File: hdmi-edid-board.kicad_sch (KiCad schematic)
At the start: 0 parts

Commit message: [#77357] Clean up schematics
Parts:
- added C1, C2: C_10u_0603, antmicro-footprints:C_0603_1608Metric, symbol antmicroCapacitors0603:C_10u_0603
- added C10, C14, C15, C16, C19, C20, C21, C22, C24, C4, C5, C6, C7, C8: C_100n_16V_X7R_0402, antmicro-footprints:C_0402_1005Metric, symbol antmicroCapacitors0402:C_100n_16V_X7R_0402
- added C11, C17, C18, C23: C_4u7_0402, antmicro-footprints:C_0402_1005Metric, symbol antmicroCapacitors0402:C_4u7_0402
- added C12, C13, C9: C_1u_0603, antmicro-footprints:C_0603_1608Metric, symbol antmicroCapacitors0603:C_1u_0603
- added C3: C_10n_0402, antmicro-footprints:C_0402_1005Metric, symbol antmicroCapacitors0402:C_10n_0402
- added D1, D3: PESD5Z5_0F, antmicro-footprints:SOD-523, symbol antmicroTVSDiodes:PESD5Z5_0F
- added D2: LED_G_0603_LTST-C190GKT, antmicro-footprints:LED_0603_1608Metric_G, symbol antmicroLEDIndicationDiscrete:LED_G_0603_LTST-C190GKT
- added D4: TPD2E009_SOT-9X3, antmicro-footprints:SOT-723, symbol antmicroTVSDiodes:TPD2E009_SOT-9X3
- added D5: BAT54-02V-G3-08, antmicro-footprints:SOD-523, symbol antmicroDiodesRectifiersSingle:BAT54-02V-G3-08
- added FB1, FB2: FB_220Z_2.2A_TDK-MPZ_0603, antmicro-footprints:FB_0603_1608Metric, symbol antmicroFerriteBeadsandChips:FB_220Z_2.2A_TDK-MPZ_0603
- added FB3, FB4: FB_600Z_0.3A_Murata-BLM15AG_0402, antmicro-footprints:FB_0402_1005Metric, symbol antmicroFerriteBeadsandChips:FB_600Z_0.3A_Murata-BLM15AG_0402
- added J1, J4: HDMI-A_WE_685119134923, antmicro-footprints:HDMI-A_Receptacle_WE_685119134923, symbol antmicroVideoConnectors:HDMI-A_WE_685119134923
- added J2, J3: PinHeader_2x2_P2.54mm_Drill1.1mm, antmicro-footprints:PinHeader_2x2_P2.54mm_Drill1.1mm, symbol antmicroGenericPinHeaders:PinHeader_2x2_P2.54mm_Drill1.1mm
- added J5: USB-C_GCT_USB4105-GF-A, antmicro-footprints:USB-C_Receptacle_GCT_USB4105-GF-A, symbol antmicroUSBConnectors:USB-C_GCT_USB4105-GF-A
- added J6: JST_SH_1x4_SM04B-SRSS-TB-LF-SN, antmicro-footprints:Conn_JST_SH_1x4_SM04B-SRSS-TB-LF-SN, symbol antmicroWire2BoardConnectors:JST_SH_1x4_SM04B-SRSS-TB-LF-SN
- added L1, L2: FB_120Z_2A_Murata-BLM18PG_0603, antmicro-footprints:FB_0603_1608Metric, symbol antmicroFerriteBeadsandChips:FB_120Z_2A_Murata-BLM18PG_0603
- added R1: R_330R_0603, antmicro-footprints:R_0603_1608Metric, symbol antmicroResistors0603:R_330R_0603
- added R10, R11: R_5k1_0402, antmicro-footprints:R_0402_1005Metric, symbol antmicroResistors0402:R_5k1_0402
- added R12: R_470R_0402, antmicro-footprints:R_0402_1005Metric, symbol antmicroResistors0402:R_470R_0402
- added R13, R14, R15: R_220R_0402, antmicro-footprints:R_0402_1005Metric, symbol antmicroResistors0402:R_220R_0402
- added R16: R_4k7_0402, antmicro-footprints:R_0402_1005Metric, symbol antmicroResistors0402:R_4k7_0402
- added R17: R_10k_0402, antmicro-footprints:R_0402_1005Metric, symbol antmicroResistors0402:R_10k_0402
- added R18: R_12k_0402, antmicro-footprints:R_0402_1005Metric, symbol antmicroResistors0402:R_12k_0402
- added R19, R2, R20, R21, R3, R4, R5, R6, R7, R8, R9: R_0R_0402, antmicro-footprints:R_0402_1005Metric, symbol antmicroResistors0402:R_0R_0402
- added TP1, TP2: TP_1.5mm_SMD, antmicro-footprints:TP_SMD_1.5mm, symbol antmicroTestPoints:TP_1.5mm_SMD
- added U1: 24LC02BT-I/SN, antmicro-footprints:SOIC-8_3.9x4.9x1.75mm_P1.27mm, symbol antmicroMemory:24LC02BT-I/SN
- added U2: 24AA024T-I/SN, antmicro-footprints:SOIC-8_3.9x4.9x1.75mm_P1.27mm, symbol antmicroMemory:24AA024T-I/SN
- added U3: NTS0302JKZ, antmicro-footprints:X2SON8_1.4x1x0.32mm_P0.35mm, symbol antmicroLogicTranslatorsLevelShifters:NTS0302JKZ
- added U4: TLV70033_SC70, antmicro-footprints:SC-70-5, symbol antmicroPMICVoltageRegulatorsLinear:TLV70033_SC70
- added U5: FT4232H_VQFN, antmicro-footprints:QFN-56-1EP_8x8mm_P0.5mm, symbol antmicroInterfaceControllers:FT4232H_VQFN
- added USB1: LED_G_0603_LG_L29K-G2J1-24-Z, antmicro-footprints:LED_0603_1608Metric_G, symbol antmicroLEDIndicationDiscrete:LED_G_0603_LG_L29K-G2J1-24-Z
- added Y1: Oscillator_12MHz_ASFLMB, antmicro-footprints:Oscillator_SMD_Abracon_ASFLMB_5x3.2x0.85mm, symbol antmicroOscillators:Oscillator_12MHz_ASFLMB
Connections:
- new net: C11.2, D5.2 (A), R15.1, U3.1 (VCC_A)
- new net: C3.1, J5.A4 (VBUS), J5.A9 (VBUS), J5.B4 (VBUS), J5.B9 (VBUS), L2.2
- new net: J5.A5 (CC_{1}), R10.1
- new net: J5.B5 (CC_{2}), R11.1
- new net: C1.2, D1.1 (C), FB1.1, J1.18 (+5V)
- new net: R12.2, USB1.1 (C)
- new net: R13.1, U3.2 (A1)
- new net: R14.1, U3.3 (A2)
- new net: R19.1, U5.22 (BDBUS0)
- new net: C2.2, D3.1 (C), FB2.2, J4.18 (+5V)
- new net: R18.1, U5.6 (REF)
- new net: R21.1, U5.24 (BDBUS2)
- new net: D2.1 (C), R1.2
- new net: R20.1, U5.23 (BDBUS1)
- new net +3V3: C10.1, C12.1, C13.1, C14.1, C15.1, C16.1, C20.1, C24.1, D5.1 (C), FB3.1, FB4.1, J6.2, U3.5 (OE), U3.8 (VCC_B), U4.5 (VOUT), U5.16 (V_{CCIO}), U5.36 (V_{CCIO}), U5.44 (V_{REGIN}), U5.50 (V_{CCIO}), Y1.1 (EN), Y1.4 (VDD)
- new net +5V: C6.1, C7.1, C8.1, C9.1, L2.1, R15.2, R16.2, R4.2, R6.2, R8.2, U4.1 (VIN), U4.3 (EN), USB1.2 (A)
- new net A0: R4.1, R5.2, U2.1 (A0)
- new net A1: R6.1, R7.2, U2.2 (A1)
- new net A2: R8.1, R9.2, U2.3 (A2)
- new net EEPROM_SCL: J2.2, R13.2, U1.6 (SCL), U2.6 (SCL)
- new net EEPROM_SDA: J2.4, R14.2, U1.5 (SDA), U2.5 (SDA)
- new net GND: C1.1, C10.2, C11.1, C12.2, C13.2, C14.2, C15.2, C16.2, C17.2, C18.1, C19.2, C2.1, C20.2, C21.2, C22.1, C23.2, C24.2, C3.2, C4.1, C5.1, C6.2, C7.2, C8.2, C9.2, D1.2 (A), D3.2 (A), D4.3, J1.11 (CKS), J1.17 (GND), J1.2 (D2S), J1.5 (D1S), J1.8 (D0S), J1.SH, J4.11 (CKS), J4.17 (GND), J4.2 (D2S), J4.5 (D1S), J4.8 (D0S), J4.SH, J5.A1 (GND), J5.A12 (GND), J5.B1 (GND), J5.B12 (GND), J6.1, J6.MP, L1.2, R1.1, R10.2, R11.2, R12.1, R17.1, R18.2, R3.1, R5.1, R7.1, R9.1, TP1.1, U1.4 (VSS), U2.4 (VSS), U3.4 (GND), U4.2 (GND), U5.10 (TEST), U5.21 (GND), U5.41 (GND), U5.45 (GND), U5.57 (GND), Y1.2 (GND)
- new net GNDREF: J5.SH, L1.1
- new net HDMI_5V: C4.2, C5.2, D2.2 (A), FB1.2, FB2.1, R2.2, TP2.1, U1.8 (VCC), U2.8 (VCC)
- new net HDMI_CEC: J1.13 (CEC), J4.13 (CEC)
- new net HDMI_CK_N: J1.12 (CK-), J4.12 (CK-)
- new net HDMI_CK_P: J1.10 (CK+), J4.10 (CK+)
- new net HDMI_D0_N: J1.9 (D0-), J4.9 (D0-)
- new net HDMI_D0_P: J1.7 (D0+), J4.7 (D0+)
- new net HDMI_D1_N: J1.6 (D1-), J4.6 (D1-)
- new net HDMI_D1_P: J1.4 (D1+), J4.4 (D1+)
- new net HDMI_D2_N: J1.3 (D2-), J4.3 (D2-)
- new net HDMI_D2_P: J1.1 (D2+), J4.1 (D2+)
- new net HDMI_HPD: J1.19 (HPD/HEAC-), J4.19 (HPD/HEAC-)
- new net HDMI_UTIL: J1.14 (UTILITY/HEAC+), J4.14 (UTILITY/HEAC+)
- new net OSCI: U5.3 (OSCI), Y1.3 (OUT)
- new net SCL: J6.4, R19.2, U3.7 (B1)
- new net SDA: J6.3, R20.2, R21.2, U3.6 (B2)
- new net SINK_SCL: J3.2, J4.15 (SCL)
- new net SINK_SDA: J3.4, J4.16 (SDA)
- new net SOURCE_SCL: J1.15 (SCL), J2.1, J3.1
- new net SOURCE_SDA: J1.16 (SDA), J2.3, J3.3
- new net USB_D_N: D4.2, J5.A7 (D_{A}-), J5.B7 (D_{B}-), U5.7 (D-)
- new net USB_D_P: D4.1, J5.A6 (D_{A}+), J5.B6 (D_{B}+), U5.8 (D+)
- new net VPHY: C17.1, C21.1, FB3.2, U5.5 (V_{PHY})
- new net VPLL: C18.2, C22.2, FB4.2, U5.9 (V_{PLL})
- new net VREGOUT: C19.1, C23.1, U5.2 (V_{CORE}), U5.31 (V_{CORE}), U5.43 (V_{REGOUT})
- new net WP: R2.1, R3.2, U1.7 (WP), U2.7 (WP)
- new net ~{RESET}: R16.1, R17.2, U5.11 (~{RESET})
- no-connect marks 0 -> 37
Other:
- removed sheet FTDI
- removed sheet HDMI
- note added: "5V -> 3.3V LDO 400mA"
- note added: "EEPROM"
- note added: "FT4232"
- note added: "HDMI SINK"
- note added: "HDMI SOURCE"
- note added: "I2C address 1 0 1 0 A0 A1 A2"
- note added: "I2C buffer"
- note added: "QWIIC"
- note added: "USB-C"

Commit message: [#77357] Update schematics, clean ERC
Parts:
- removed D2: LED_G_0603_LTST-C190GKT, antmicro-footprints:LED_0603_1608Metric_G, symbol antmicroLEDIndicationDiscrete:LED_G_0603_LTST-C190GKT
- removed J2, J3: PinHeader_2x2_P2.54mm_Drill1.1mm, antmicro-footprints:PinHeader_2x2_P2.54mm_Drill1.1mm, symbol antmicroGenericPinHeaders:PinHeader_2x2_P2.54mm_Drill1.1mm
- removed R1: R_330R_0603, antmicro-footprints:R_0603_1608Metric, symbol antmicroResistors0603:R_330R_0603
- removed R12: R_470R_0402, antmicro-footprints:R_0402_1005Metric, symbol antmicroResistors0402:R_470R_0402
- removed R2, R3, R4, R5, R6, R7, R8, R9: R_0R_0402, antmicro-footprints:R_0402_1005Metric, symbol antmicroResistors0402:R_0R_0402
- removed USB1: LED_G_0603_LG_L29K-G2J1-24-Z, antmicro-footprints:LED_0603_1608Metric_G, symbol antmicroLEDIndicationDiscrete:LED_G_0603_LG_L29K-G2J1-24-Z
- added C25, C27, C29: C_100n_16V_X7R_0402, antmicro-footprints:C_0402_1005Metric, symbol antmicroCapacitors0402:C_100n_16V_X7R_0402
- added C26, C28: C_10u_0603, antmicro-footprints:C_0603_1608Metric, symbol antmicroCapacitors0603:C_10u_0603
- added D10, D6, D7, D8, D9: PUSB3F96X_PASS, antmicro-footprints:Nexperia_DFN-10_2.5x1mm_P0.5mm, symbol antmicroTVSDiodes:PUSB3F96X_PASS
- added D11, D2: LED_G_0603_LG_L29K-G2J1-24-Z, antmicro-footprints:LED_0603_1608Metric_G, symbol antmicroLEDIndicationDiscrete:LED_G_0603_LG_L29K-G2J1-24-Z
- added J7: PinHeader_2x3_P2.54mm_Drill1.1mm, antmicro-footprints:PinHeader_2x3_P2.54mm_Drill1.1mm, symbol antmicroGenericPinHeaders:PinHeader_2x3_P2.54mm_Drill1.1mm
- added R1, R12: R_560R_0402, antmicro-footprints:R_0402_1005Metric, symbol antmicroResistors0402:R_560R_0402
- added R2, R3, R4, R5, R6, R7, R8, R9: R_10k_0402, antmicro-footprints:R_0402_1005Metric, symbol antmicroResistors0402:R_10k_0402
- added U6: TPS2117DRLR, antmicro-footprints:SOT-583, symbol antmicroPMICPowerDistributionSwitchesLoadDrivers:TPS2117DRLR
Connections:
- net +3V3: now also C25.2
- net +5V: now also C28.2, C29.2, D11.2 (A), U6.6 (VIN2)
- net A0: now also R4.1, R5.2
- net A1: now also R6.1, R7.2
- net A2: now also R8.1, R9.2
- net EEPROM_SCL: now also D10.4 (CH3), D10.7 (CH3), J7.6
- net EEPROM_SDA: now also D10.5 (CH4), D10.6 (CH4), J7.5
- net GND: now also C25.1, C26.1, C27.1, C28.1, C29.1, D10.3 (GND), D10.8 (GND), D6.3 (GND), D6.8 (GND), D7.3 (GND), D7.8 (GND), D8.3 (GND), D8.8 (GND), D9.3 (GND), D9.8 (GND), R1.1, R12.2, R3.1, R5.1, R7.1, R9.1, U6.1 (GND), U6.4 (PR1), U6.5 (MODE)
- net HDMI_5V: now also C26.2, C27.2, D2.2 (A), U6.3 (VIN1); no longer C4.2, C5.2, U1.8 (VCC), U2.8 (VCC)
- net HDMI_CEC: now also D8.2 (CH2), D8.9 (CH2)
- net HDMI_CK_N: now also D7.5 (CH4), D7.6 (CH4)
- net HDMI_CK_P: now also D7.4 (CH3), D7.7 (CH3)
- net HDMI_D0_N: now also D7.2 (CH2), D7.9 (CH2)
- net HDMI_D0_P: now also D7.1 (CH1), D7.10 (CH1)
- net HDMI_D1_N: now also D6.5 (CH4), D6.6 (CH4)
- net HDMI_D1_P: now also D6.4 (CH3), D6.7 (CH3)
- net HDMI_D2_N: now also D6.2 (CH2), D6.9 (CH2)
- net HDMI_D2_P: now also D6.1 (CH1), D6.10 (CH1)
- net HDMI_HPD: now also D8.1 (CH1), D8.10 (CH1)
- net HDMI_UTIL: now also D9.1 (CH1), D9.10 (CH1)
- net SCL: now also D10.2 (CH2), D10.9 (CH2)
- net SDA: now also D10.1 (CH1), D10.10 (CH1)
- net SINK_SCL: now also D9.2 (CH2), D9.9 (CH2), J7.2
- net SINK_SDA: now also D9.4 (CH3), D9.7 (CH3), J7.1
- net SOURCE_SCL: now also D8.4 (CH3), D8.7 (CH3), J7.4
- net SOURCE_SDA: now also D8.5 (CH4), D8.6 (CH4), J7.3
- net WP: now also R2.1, R3.2
- new net: D2.1 (C), R1.2
- new net: D11.1 (C), R12.1
- new net: D9.5 (CH4), D9.6 (CH4)
- new net EEPROM_5V: C4.2, C5.2, R2.2, R4.2, R6.2, R8.2, U1.8 (VCC), U2.8 (VCC), U6.2 (VOUT), U6.7 (VOUT)
- no-connect marks 37 -> 39
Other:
- note added: "7bit I2C address 0x50"
- note added: "7bit I2C address default set to 0x50"
- note added: "POWER MUX"
- moved on the sheet: C1, C10, C11, C12, C13, C14, C15, C16, C17, C18, C19, C2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

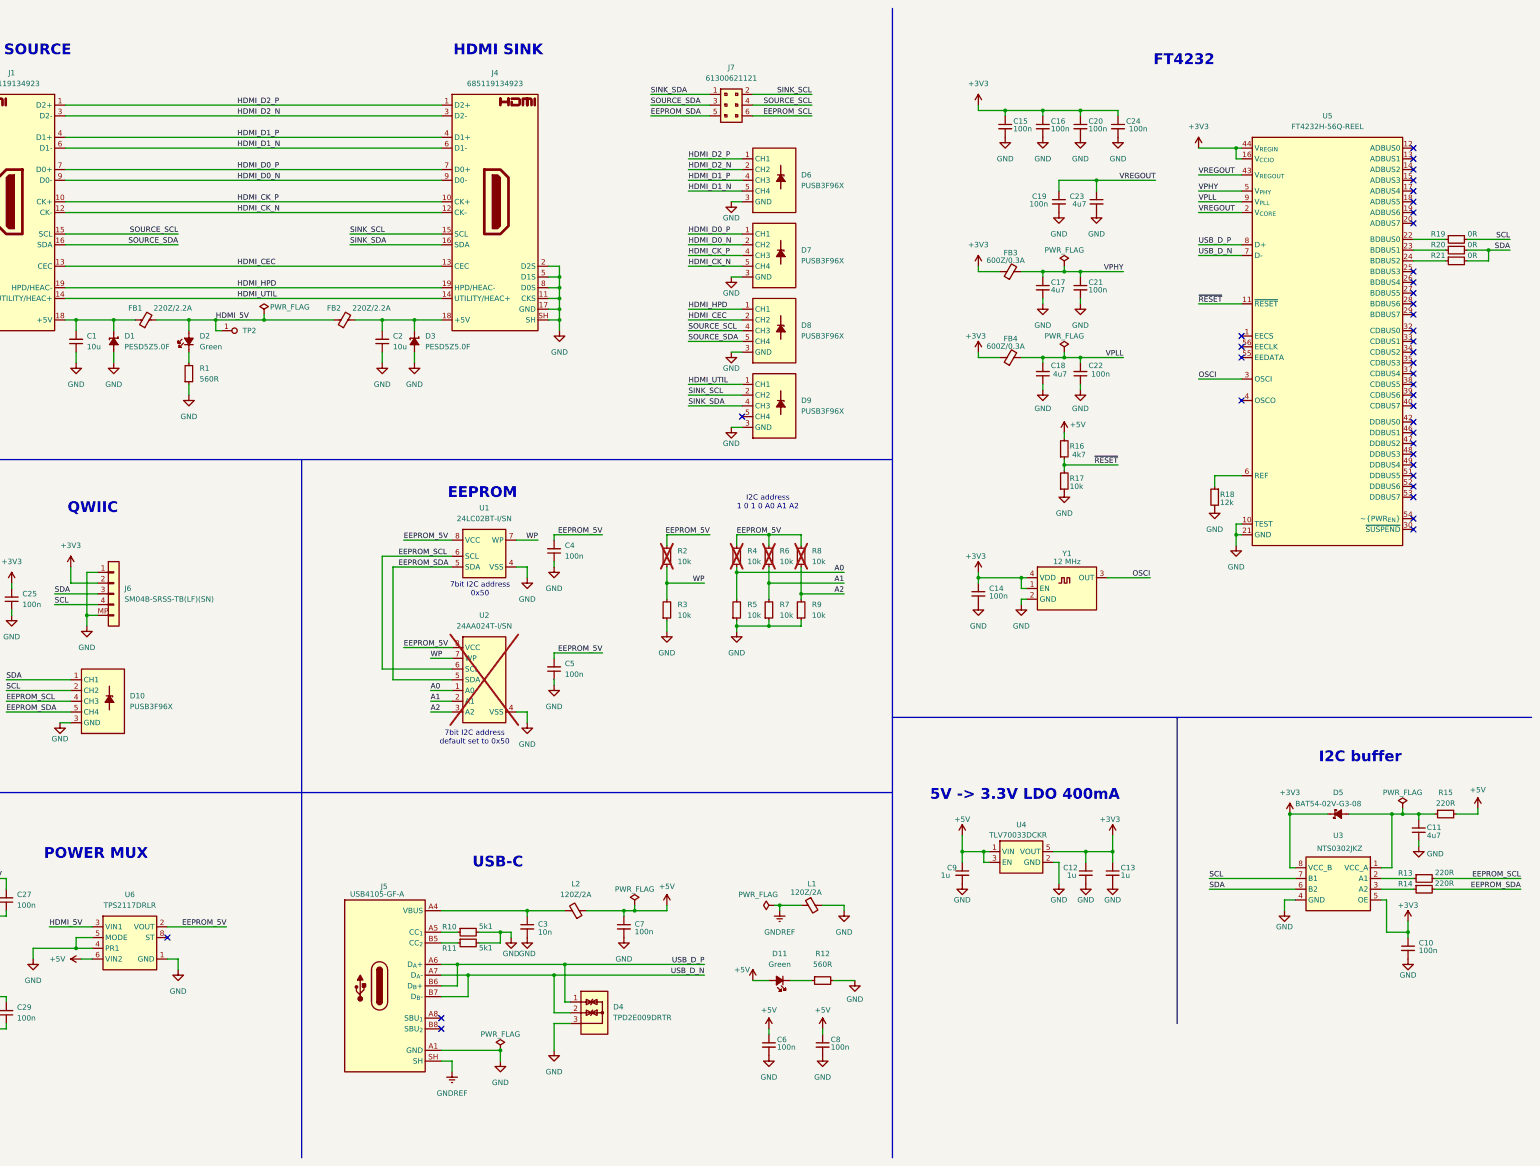
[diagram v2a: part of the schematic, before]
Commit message: [#77357] Place components on PCB
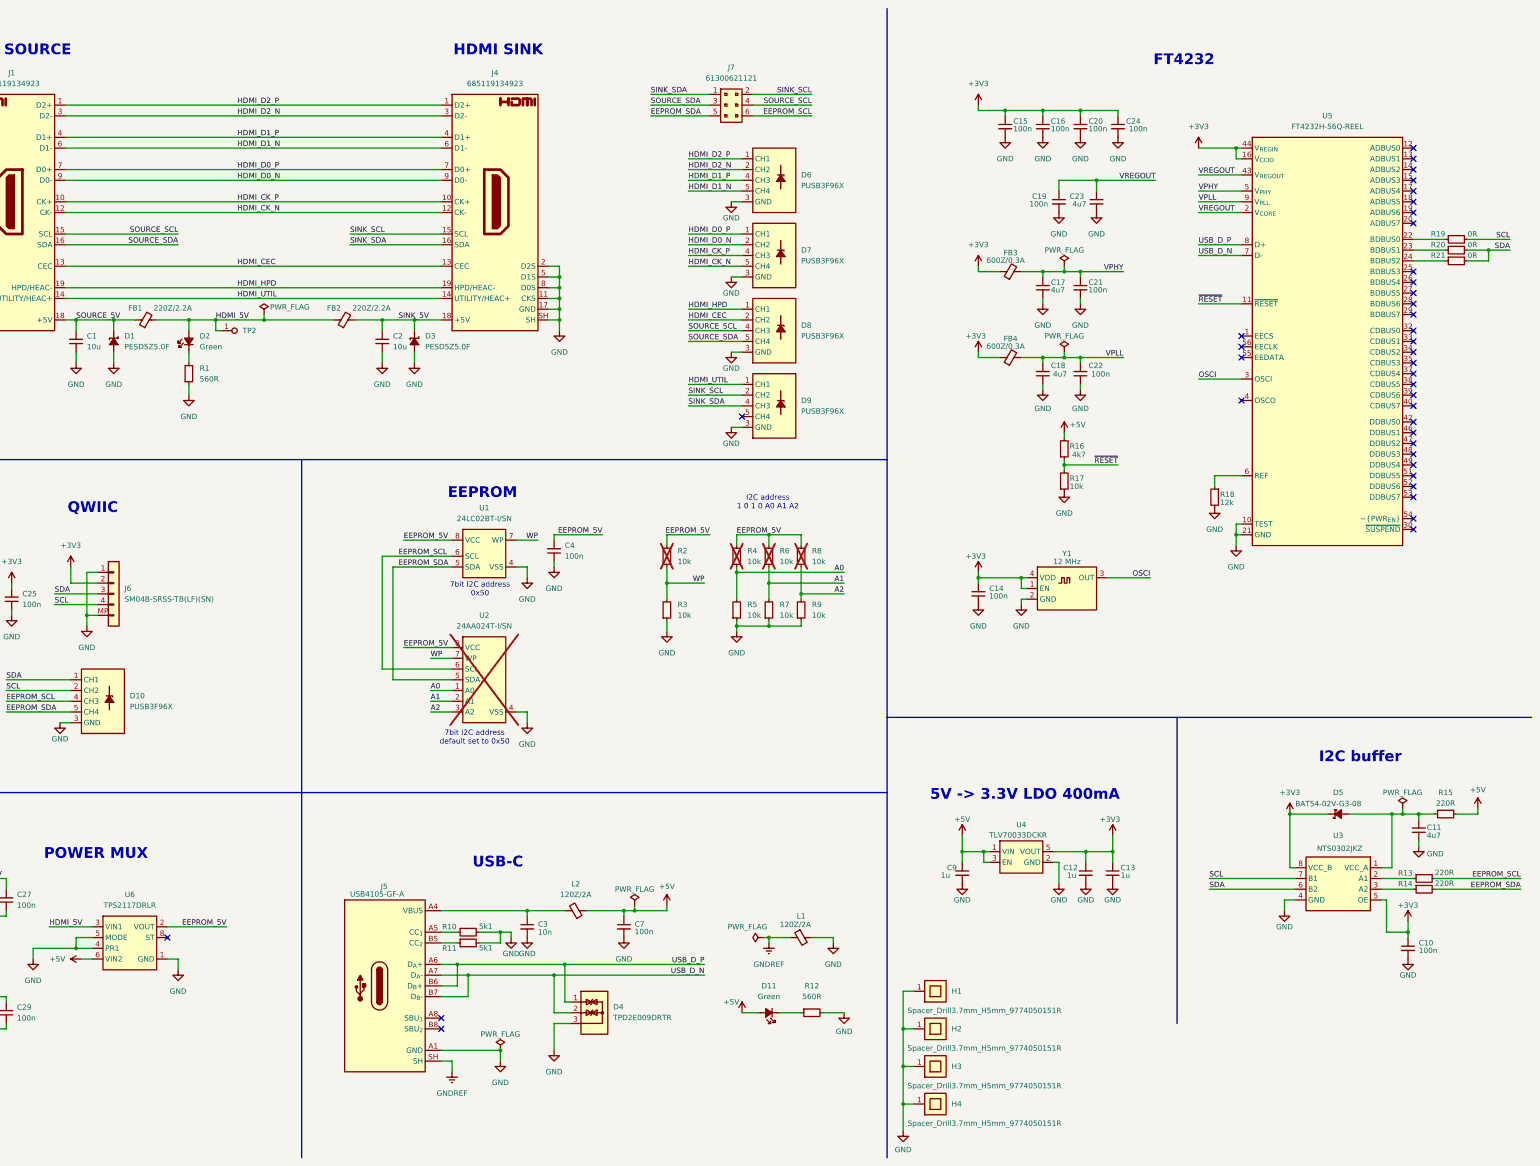
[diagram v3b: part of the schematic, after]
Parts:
- removed C5, C6, C8: C_100n_16V_X7R_0402, antmicro-footprints:C_0402_1005Metric, symbol antmicroCapacitors0402:C_100n_16V_X7R_0402
- added H1, H2, H3, H4: Spacer_Drill3.7mm_H5mm_9774050151R, antmicro-footprints:Spacer_Drill3.7mm_H5mm_9774050151R, symbol antmicroMechanicalParts:Spacer_Drill3.7mm_H5mm_9774050151R
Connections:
- net GND: now also H1.1, H2.1, H3.1, H4.1
- net SOURCE_5V: now reaches C1.2, D1.1 (C), FB1.1, J1.18 (+5V)
- net SINK_5V: now reaches C2.2, D3.1 (C), FB2.2, J4.18 (+5V)
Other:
- moved on the sheet: D11, L1, R12
